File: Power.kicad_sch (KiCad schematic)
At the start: 26 parts, among them Q601 AO3401A, U601 HT7463A, U602 BD2243G, U603 MIC5504-3.3YM5

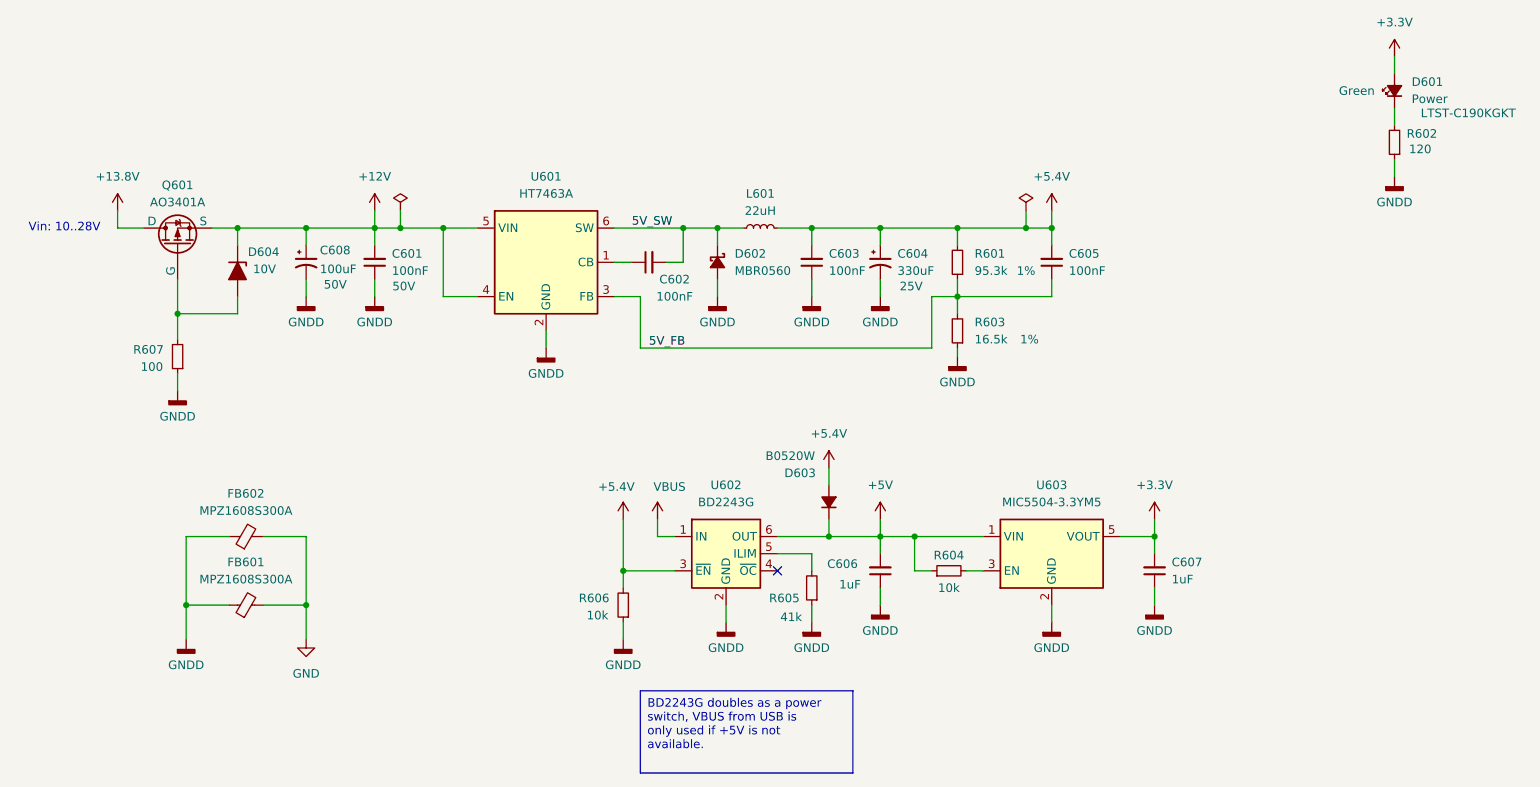
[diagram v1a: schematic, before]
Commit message: A0 Production. Updated to KiCad 9.0.x
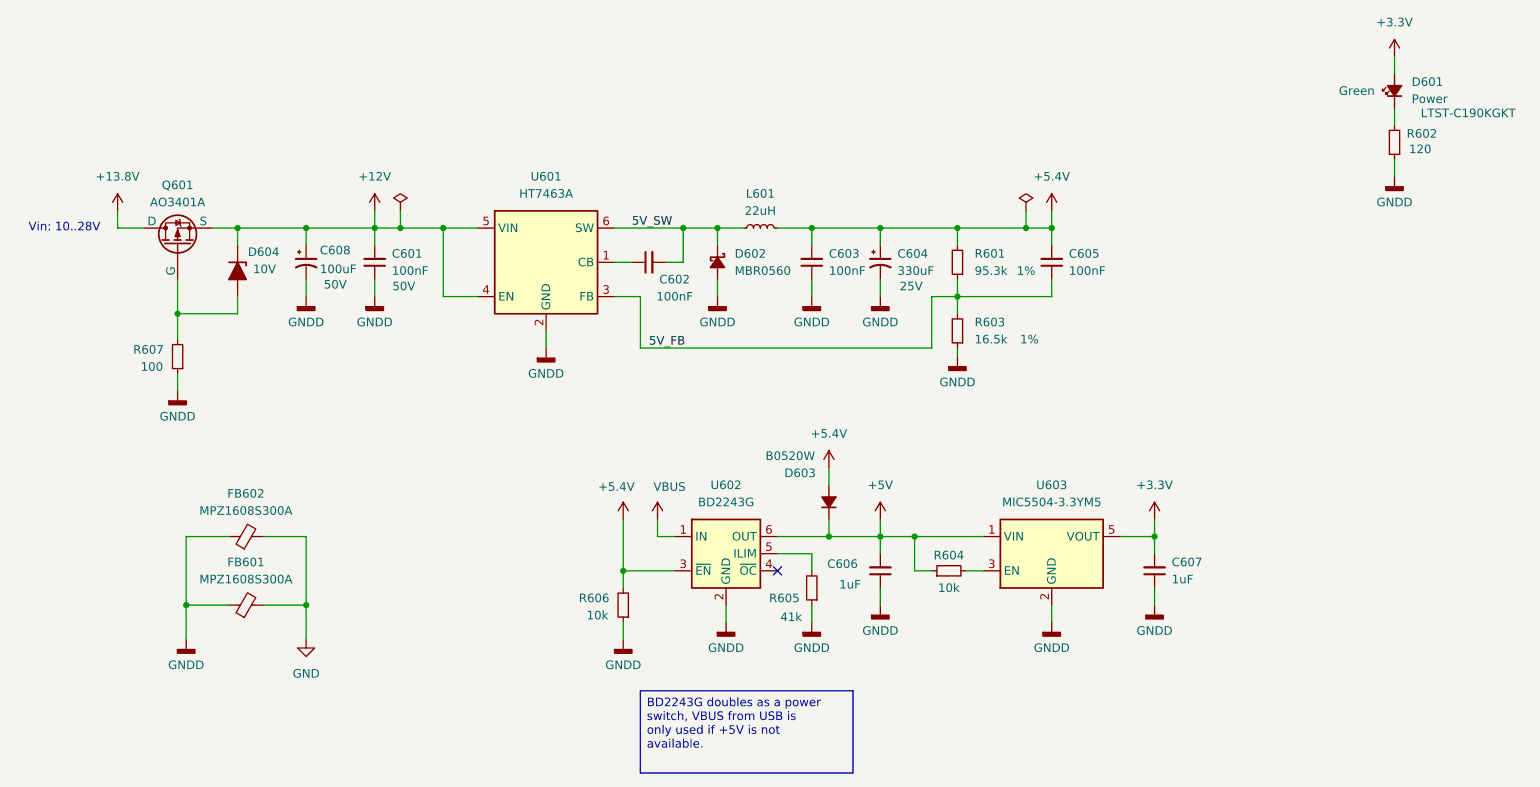
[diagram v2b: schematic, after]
